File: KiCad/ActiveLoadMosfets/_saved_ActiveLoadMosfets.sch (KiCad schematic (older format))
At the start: 68 parts, among them J1 Conn_01x02_Male, J2 Conn_02x03_Odd_Even, Q1 STP60NF06L, Q2 STP60NF06L, Q3 STP60NF06L, Q4 STP60NF06L, Q5 STP60NF06L, Q6 STP60NF06L, Q7 IRLML2244, Q8 IRLML2244, Q9 IRLML2244, SW1 SW_SPST, SW2 SW_SPDT, U1 TLV2372, U2 LM78M12, U3 ATxmega32E5-AU, U4 LED-3digits, U5 LM78M33, U6 SCT2167, U7 SCT2167, U8 LED-3digits

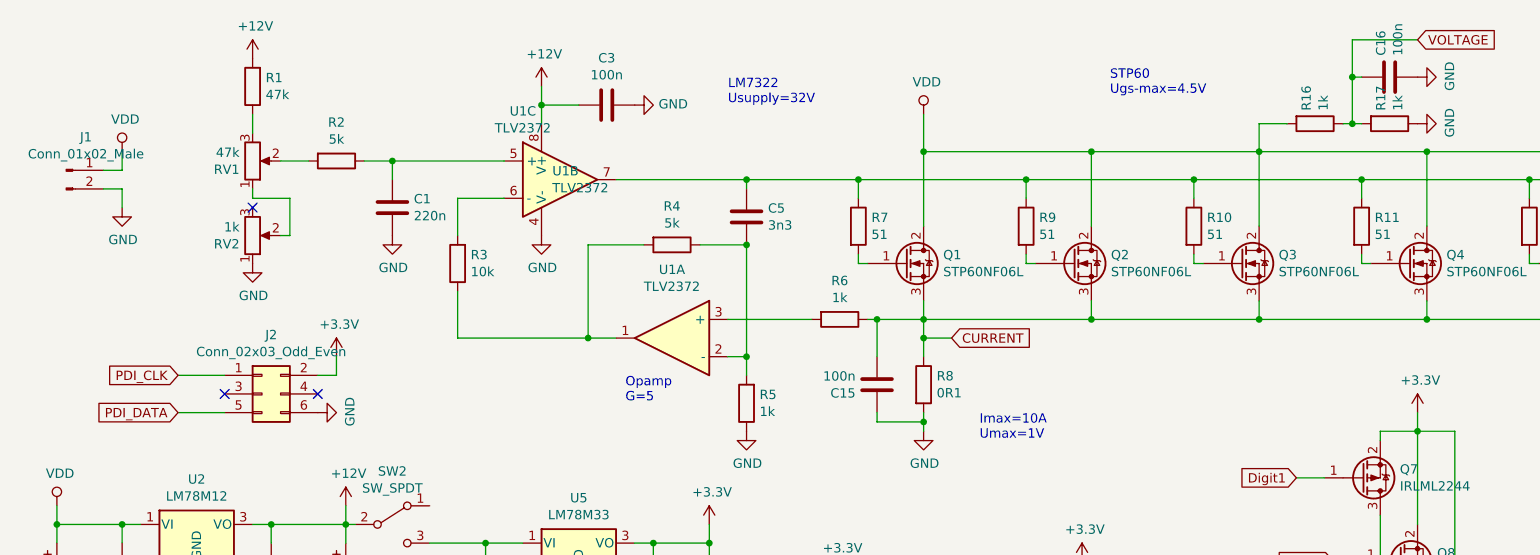
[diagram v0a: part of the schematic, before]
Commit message: New Atmel Studio project for ActiveLoadMosfets
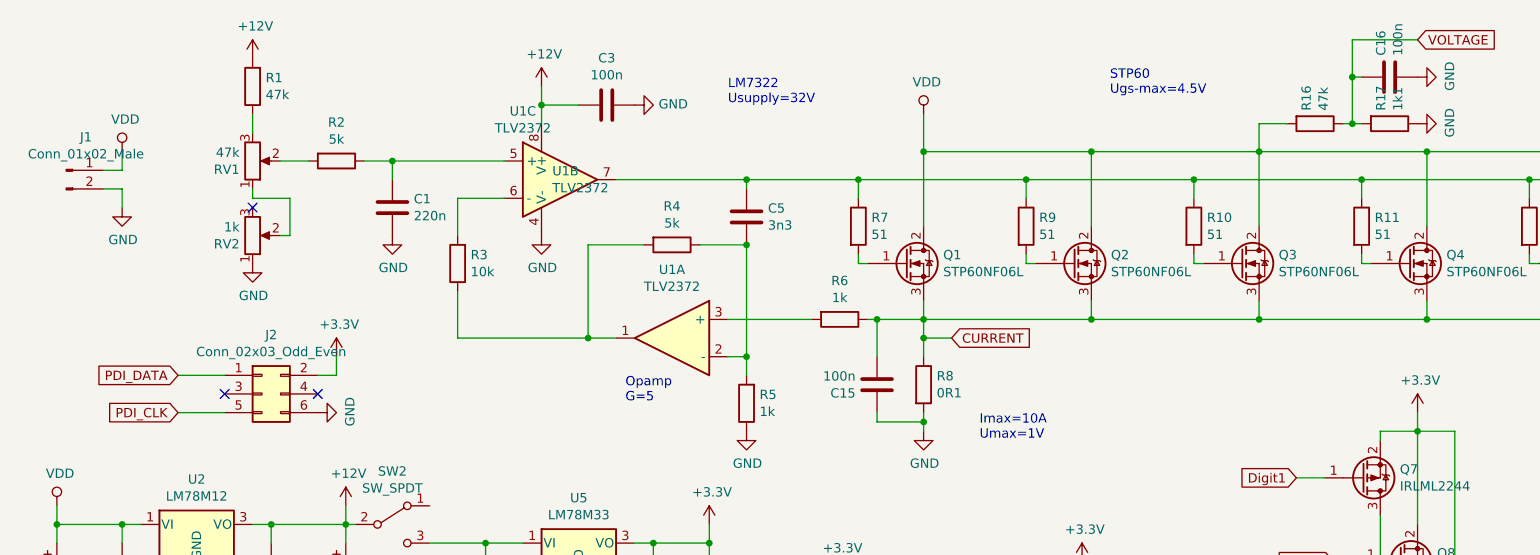
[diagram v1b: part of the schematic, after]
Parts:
- R16: value 1k -> 47k
- R17: value 1k -> 1k1
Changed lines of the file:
@@
 Wire Wire Line
 	2300 2400 2200 2400
+Text GLabel 1450 2600 0    50   Input ~ 0
+PDI_CLK
 Text GLabel 1450 2400 0    50   Input ~ 0
-PDI_CLK
-Text GLabel 1450 2600 0    50   Input ~ 0
 PDI_DATA
 Wire Wire Line
@@
 P 7550 1050
 F 0 "R16" H 7480 1004 50  0000 R CNN
-F 1 "1k" H 7480 1095 50  0000 R CNN
+F 1 "47k" H 7480 1095 50  0000 R CNN
 F 2 "Resistors_SMD:R_0805" V 7480 1050 50  0001 C CNN
 F 3 "~" H 7550 1050 50  0001 C CNN
@@
 P 7950 1050
 F 0 "R17" H 7880 1004 50  0000 R CNN
-F 1 "1k" H 7880 1095 50  0000 R CNN
+F 1 "1k1" H 7880 1095 50  0000 R CNN
 F 2 "Resistors_SMD:R_0805" V 7880 1050 50  0001 C CNN
 F 3 "~" H 7950 1050 50  0001 C CNN

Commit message: More c++ code, bug fixes on the PCB
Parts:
- added C21: 10u, Capacitors_SMD:CP_Elec_4x5.8, symbol Device:CP
- added R24: 1k1, Resistors_SMD:R_0805, symbol Device:R
- C5: value 3n3 -> 1n
- R15, R19: value 1k -> 5k
- R4: value 5k -> 5k / 47k ?
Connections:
- wire segments 226 -> 229
- no-connect marks 19 -> 20
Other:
- moved on the sheet: C5
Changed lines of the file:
@@
 	1    0    0    -1
 $EndComp
-Text Notes 5750 2750 0    50   ~ 0
+Text Notes 5550 2750 0    50   ~ 0
 Imax=10A\nUmax=1V
 Text Notes 4400 950  0    50   ~ 0
@@
 P 4100 1700
 F 0 "R4" V 3893 1700 50  0000 C CNN
-F 1 "5k" V 3984 1700 50  0000 C CNN
+F 1 "5k / 47k ?" V 3984 1700 50  0000 C CNN
 F 2 "Resistors_SMD:R_0805" V 4030 1700 50  0001 C CNN
 F 3 "~" H 4100 1700 50  0001 C CNN
@@
 Wire Wire Line
 	2950 2200 2950 1950
-Wire Wire Line
-	3800 1350 4500 1350
 Connection ~ 5100 1350
 $Comp
 L Device:C C5
 U 1 1 5B75BACA
-P 4500 1550
-F 0 "C5" H 4615 1596 50  0000 L CNN
-F 1 "3n3" H 4615 1505 50  0000 L CNN
-F 2 "Capacitors_SMD:C_0805" H 4538 1400 50  0001 C CNN
-F 3 "~" H 4500 1550 50  0001 C CNN
-	1    4500 1550
-	1    0    0    -1
-$EndComp
-Wire Wire Line
-	4500 1400 4500 1350
-Connection ~ 4500 1350
-Wire Wire Line
-	4500 1350 5100 1350
+P 4700 1500
+F 0 "C5" H 4815 1546 50  0000 L CNN
+F 1 "1n" H 4815 1455 50  0000 L CNN
+F 2 "Capacitors_SMD:C_0805" H 4738 1350 50  0001 C CNN
+F 3 "~" H 4700 1500 50  0001 C CNN
+	1    4700 1500
+	1    0    0    -1
+$EndComp
 $Comp
 L Device:R R2
@@
 Wire Wire Line
 	4500 1700 4500 2300
-Connection ~ 4500 1700
 Connection ~ 4500 2300
 $Comp
@@
 P 6300 6150
 F 0 "R15" H 6230 6104 50  0000 R CNN
-F 1 "1k" H 6230 6195 50  0000 R CNN
+F 1 "5k" H 6230 6195 50  0000 R CNN
 F 2 "Resistors_SMD:R_0805" V 6230 6150 50  0001 C CNN
 F 3 "~" H 6300 6150 50  0001 C CNN
@@
 Wire Wire Line
 	5200 2100 5450 2100
-Text GLabel 5600 2200 2    50   Input ~ 0
+Text GLabel 6200 2200 2    50   Input ~ 0
 CURRENT
 Wire Wire Line
@@
 P 8900 6150
 F 0 "R19" H 8830 6104 50  0000 R CNN
-F 1 "1k" H 8830 6195 50  0000 R CNN
+F 1 "5k" H 8830 6195 50  0000 R CNN
 F 2 "Resistors_SMD:R_0805" V 8830 6150 50  0001 C CNN
 F 3 "~" H 8900 6150 50  0001 C CNN
@@
 Wire Wire Line
 	2350 3200 2400 3200
+Connection ~ 4700 1350
+Wire Wire Line
+	4700 1350 5100 1350
+Connection ~ 2950 1650
+Wire Wire Line
+	3800 1350 4700 1350
+Wire Wire Line
+	2950 1650 4700 1650
+$Comp
+L Device:R R24
+U 1 1 5B9E9754
+P 5750 2200
+F 0 "R24" V 5543 2200 50  0000 C CNN
+F 1 "1k1" V 5634 2200 50  0000 C CNN
+F 2 "Resistors_SMD:R_0805" V 5680 2200 50  0001 C CNN
+F 3 "~" H 5750 2200 50  0001 C CNN
+	1    5750 2200
+	0    1    1    0
+$EndComp
+$Comp
+L Device:CP C21
+U 1 1 5B9E9EC7
+P 6050 2400
+F 0 "C21" H 6168 2446 50  0000 L CNN
+F 1 "10u" H 6168 2355 50  0000 L CNN
+F 2 "Capacitors_SMD:CP_Elec_4x5.8" H 6088 2250 50  0001 C CNN
+F 3 "~" H 6050 2400 50  0001 C CNN
+	1    6050 2400
+	1    0    0    -1
+$EndComp
+NoConn ~ 5450 2800
+$Comp
+L power:GND #PWR0132
+U 1 1 5BA11FCB
+P 6050 2550
+F 0 "#PWR0132" H 6050 2300 50  0001 C CNN
+F 1 "GND" H 6055 2377 50  0000 C CNN
+F 2 "" H 6050 2550 50  0001 C CNN
+F 3 "" H 6050 2550 50  0001 C CNN
+	1    6050 2550
+	1    0    0    -1
+$EndComp
+Wire Wire Line
+	5900 2200 6050 2200
+Wire Wire Line
+	6050 2200 6050 2250
+Wire Wire Line
+	6050 2200 6200 2200
+Connection ~ 6050 2200
 $EndSCHEMATC
